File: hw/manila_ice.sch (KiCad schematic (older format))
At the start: 22 parts, among them J1 USB_B, U9 SRV05-4

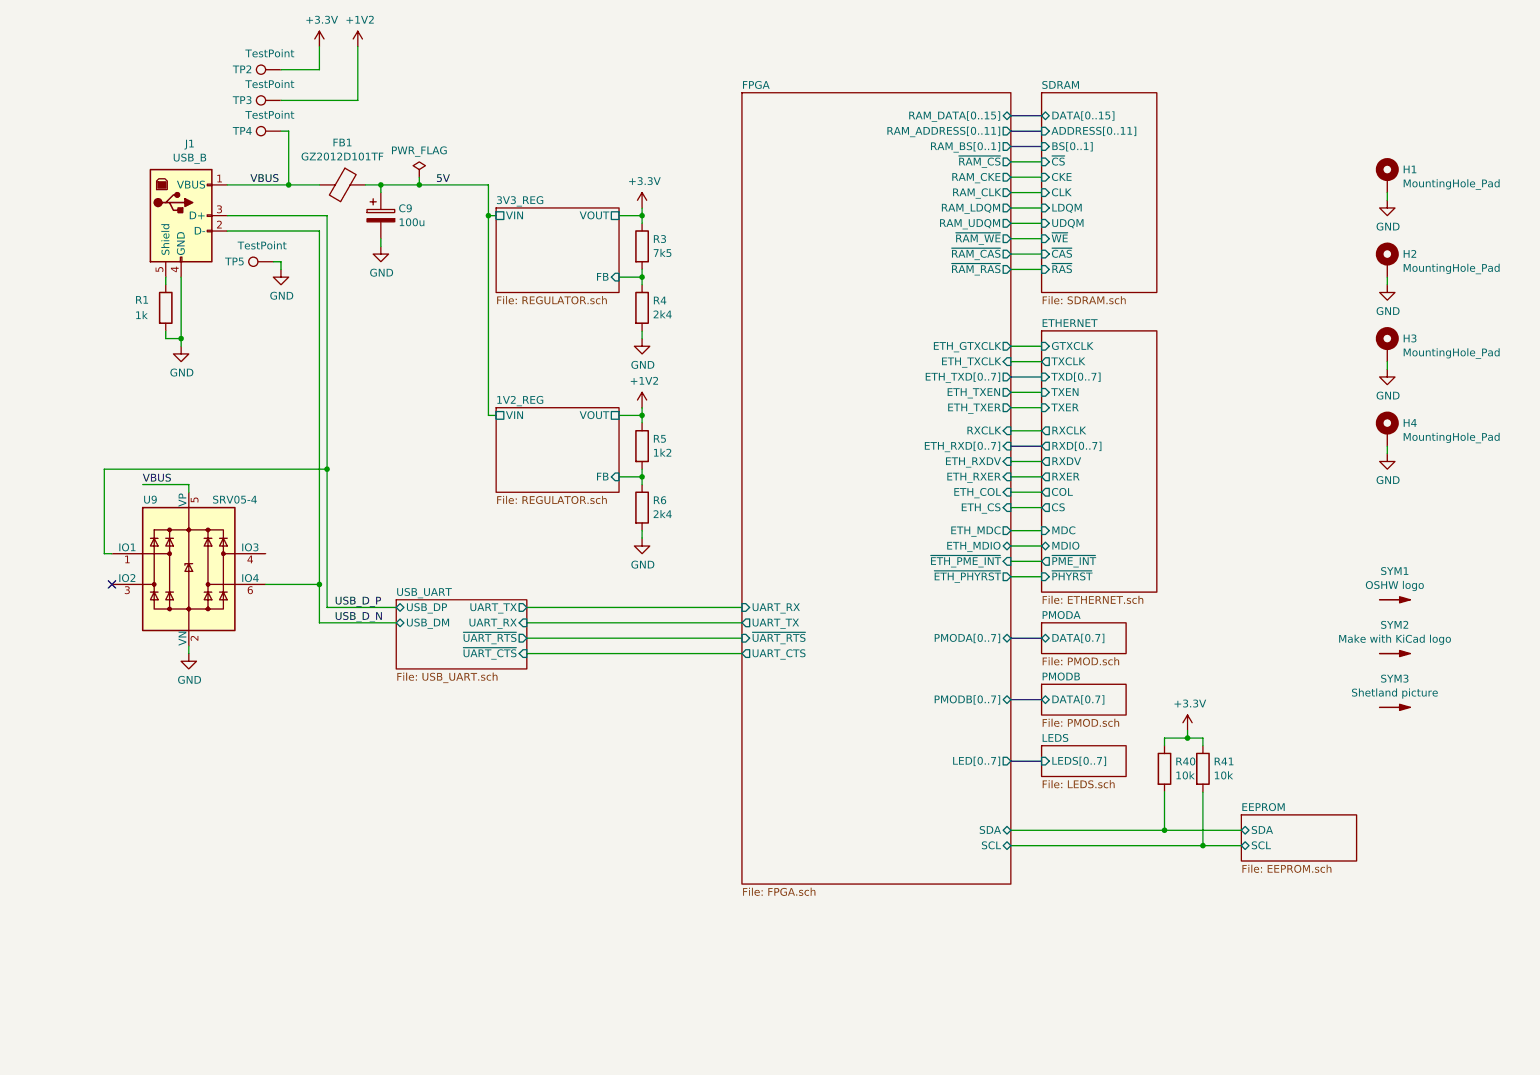
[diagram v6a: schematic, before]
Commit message: Update schematic to change slew rates of PSUs and to add switch debouncing
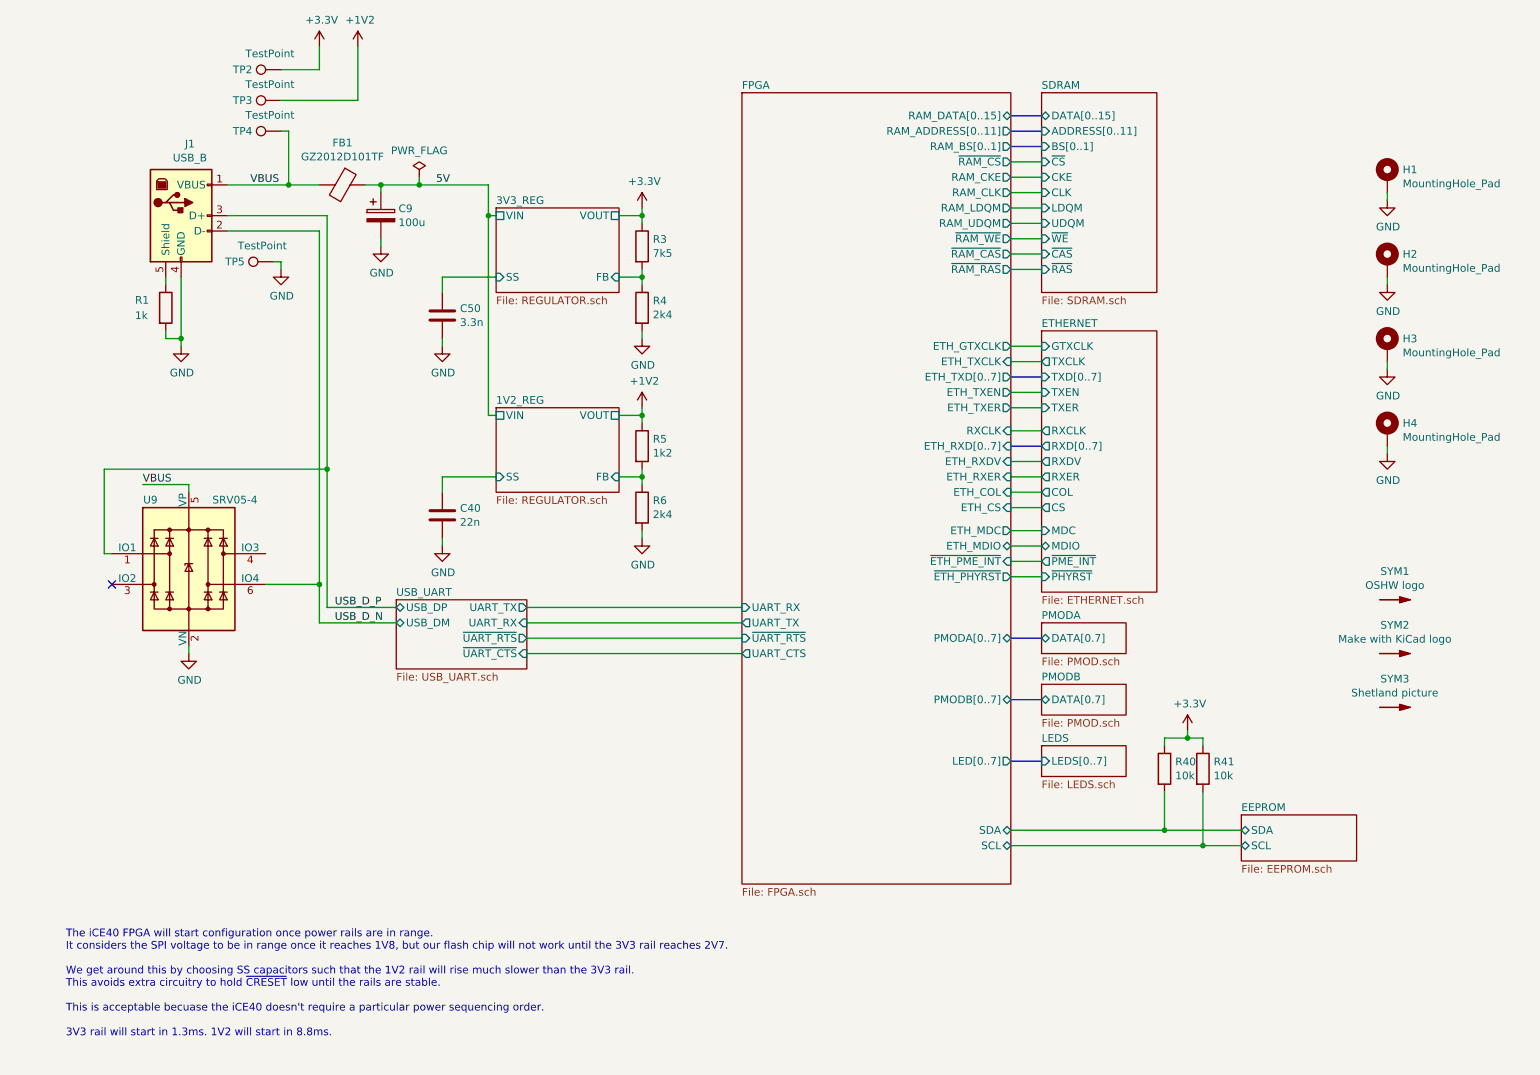
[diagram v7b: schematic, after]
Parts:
- added C40: 22n, Capacitor_SMD:C_0603_1608Metric, symbol Device:C
- added C50: 3.3n, Capacitor_SMD:C_0603_1608Metric, symbol Device:C
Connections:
- net GND: now also C40.2, C50.2
- new net 1V2_REG/SS: C40.1
- new net 3V3_REG/SS: C50.1
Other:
- note added: "The iCE40 FPGA will start configuration once power rails are in range.\nIt considers the SPI voltage to be in range once it reaches 1V8, but our flash chip will not work until the 3V3 rail reaches 2V7.\n\nWe get around this by choosing SS capacitors such that the 1V2 rail will rise much slower than the 3V3 rail.\nThis avoids extra circuitry to hold ~CRESET~ low until the rails are stable.\n\nThis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"

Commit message: Schematic tweaks
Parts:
- removed C40: 22n, Capacitor_SMD:C_0603_1608Metric, symbol Device:C
- removed C50: 3.3n, Capacitor_SMD:C_0603_1608Metric, symbol Device:C
- added R45: 360k, Resistor_SMD:R_0603_1608Metric, symbol Device:R
- added R46: 180k, Resistor_SMD:R_0603_1608Metric, symbol Device:R
- added R48: 10k, Resistor_SMD:R_0603_1608Metric, symbol Device:R
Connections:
- net +3V3: now also R45.1, R48.1
- net GND: now also R46.2
- new net 1V2_REG/EN: R45.2, R46.1
- new net EEPROM/~WC: R48.2
- no-connect marks 1 -> 2
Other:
- note added: "The iCE40 FPGA will start configuration once power rails are in range.\nIt considers the SPI voltage to be in range once it reaches 1V8, but our flash chip will not work until the 3V3 rail reaches 2V7.\n\nWe get around this by sequencing the 1V2 rail to only come up after the 3V3 is good. This avoids extra circuitry to hold ~CRESET~ low until the rails are stable.\n\nThis is acceptable becuase th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"
- note removed: "The iCE40 FPGA will start configuration once power rails are in range.\nIt considers the SPI voltage to be in range once it reaches 1V8, but our flash chip will not work until the 3V3 rail reaches 2V7.\n\nWe get around this by choosing SS capacitors such that the 1V2 rail will rise much slower than the 3V3 rail.\nThis avoids extra circuitry to hold ~CRESET~ low until the rails are stable.\n\nThis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"
- moved on the sheet: R41
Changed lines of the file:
@@
 encoding utf-8
 Sheet 1 11
-Title ""
+Title "manila iCE"
 Date ""
-Rev ""
+Rev "1.0"
 Comp ""
 Comment1 ""
@@
 F35 "SDA" B R 7000 5800 50
 F36 "SCL" B R 7000 5900 50
+F37 "~WC" O R 7000 6000 50
 $EndSheet
 $Sheet
@@
 $EndSheet
 $Sheet
-S 8500 5700 750  300
+S 8900 5700 750  400
 U 5DAA4BA2
 F0 "EEPROM" 50
 F1 "EEPROM.sch" 50
-F2 "SDA" B L 8500 5800 50
-F3 "SCL" B L 8500 5900 50
+F2 "SDA" B L 8900 5800 50
+F3 "SCL" B L 8900 5900 50
+F4 "~WC" I L 8900 6000 50
 $EndSheet
 $Sheet
@@
 F3 "VOUT" U R 4450 3100 50
 F4 "VIN" U L 3650 3100 50
-F5 "SS" I L 3650 3500 50
-$EndSheet
-$Sheet
-S 3650 1750 800  550
-U 5DB28A3C
-F0 "3V3_REG" 50
-F1 "REGULATOR.sch" 50
-F2 "FB" I R 4450 2200 50
-F3 "VOUT" U R 4450 1800 50
-F4 "VIN" U L 3650 1800 50
-F5 "SS" I L 3650 2200 50
+F5 "EN" I L 3650 3500 50
 $EndSheet
 $Comp
@@
 L Device:R R?
 U 1 1 5DAF8A15
-P 8250 5400
+P 8300 5400
 AR Path="/5D7C5FBE/5DAF8A15" Ref="R?"  Part="1"
 AR Path="/5DAF8A15" Ref="R41"  Part="1"
-F 0 "R41" H 8320 5446 50  0000 L CNN
-F 1 "10k" H 8320 5355 50  0000 L CNN
-F 2 "Resistor_SMD:R_0603_1608Metric" V 8180 5400 50  0001 C CNN
-F 3 "~" H 8250 5400 50  0001 C CNN
-F 4 "0" H 8320 5546 50  0001 C CNN "JLCPCB Rotation"
-F 5 "C25804" H 8320 5546 50  0001 C CNN "LCSC Part"
-	1    8250 5400
+F 0 "R41" H 8370 5446 50  0000 L CNN
+F 1 "10k" H 8370 5355 50  0000 L CNN
+F 2 "Resistor_SMD:R_0603_1608Metric" V 8230 5400 50  0001 C CNN
+F 3 "~" H 8300 5400 50  0001 C CNN
+F 4 "0" H 8370 5546 50  0001 C CNN "JLCPCB Rotation"
+F 5 "C25804" H 8370 5546 50  0001 C CNN "LCSC Part"
+	1    8300 5400
 	1    0    0    -1
 $EndComp
@@
 	8000 5200 8150 5200
 Wire Wire Line
-	8250 5200 8250 5250
+	8300 5200 8300 5250
 Wire Wire Line
 	8150 5150 8150 5200
 Wire Wire Line
-	8150 5200 8250 5200
+	8150 5200 8300 5200
 Wire Wire Line
 	7000 5800 8000 5800
 Wire Wire Line
-	8500 5900 8250 5900
-Wire Wire Line
 	8000 5550 8000 5800
 Wire Wire Line
-	8000 5800 8500 5800
-Wire Wire Line
-	8250 5550 8250 5900
-Wire Wire Line
-	8250 5900 7000 5900
+	8000 5800 8900 5800
 Wire Wire Line
 	4600 3900 4600 3850
@@
 Connection ~ 8150 5200
 Connection ~ 8000 5800
-Connection ~ 8250 5900
 Connection ~ 4600 3100
 Connection ~ 4600 3500
@@
 Connection ~ 2550 3450
 NoConn ~ 1150 4200
-$Comp
-L Device:C C?
-U 1 1 5DBEC469
-P 3300 3750
-AR Path="/5D7E2E67/5DBEC469" Ref="C?"  Part="1"
-AR Path="/5DAFE486/5DBEC469" Ref="C?"  Part="1"
-AR Path="/5DB28A3C/5DBEC469" Ref="C?"  Part="1"
-AR Path="/5DBEC469" Ref="C40"  Part="1"
-F 0 "C40" H 3415 3796 50  0000 L CNN
-F 1 "22n" H 3415 3705 50  0000 L CNN
-F 2 "Capacitor_SMD:C_0603_1608Metric" H 3338 3600 50  0001 C CNN
-F 3 "~" H 3300 3750 50  0001 C CNN
-F 4 "0" H 3415 3896 50  0001 C CNN "JLCPCB Rotation"
-F 5 "C21122" H 3415 3896 50  0001 C CNN "LCSC Part"
-	1    3300 3750
-	1    0    0    -1
-$EndComp
-$Comp
-L power:GND #PWR?
-U 1 1 5DBEC46F
-P 3300 3950
-AR Path="/5DBEC46F" Ref="#PWR?"  Part="1"
-AR Path="/5D7E2E67/5DBEC46F" Ref="#PWR?"  Part="1"
-AR Path="/5DAFE486/5DBEC46F" Ref="#PWR?"  Part="1"
-AR Path="/5DB28A3C/5DBEC46F" Ref="#PWR?"  Part="1"
-F 0 "#PWR?" H 3300 3700 50  0001 C CNN
-F 1 "GND" H 3305 3777 50  0000 C CNN
-F 2 "" H 3300 3950 50  0001 C CNN
-F 3 "" H 3300 3950 50  0001 C CNN
-	1    3300 3950
-	1    0    0    -1
-$EndComp
-Wire Wire Line
-	3300 3950 3300 3900
-Text Notes 850  7150 0    50   ~ 0
-The iCE40 FPGA will start configuration once power rails are in range.\nIt considers the SPI voltage to be in range once it reaches 1V8, but our flash chip will not work until the 3V3 rail reaches 2V7.\n\nWe get around this by choosing SS capacitors such that the 1V2 rail will rise much slower than the 3V3 rail.\nThis avoids extra circuitry to hold ~CRESET~ low until the rails are stable.\n\nThis is acceptable becuase the iCE40 doesn't require a particular power sequencing order.\n\n3V3 rail will start in 1.3ms. 1V2 will start in 8.8ms.
-Wire Wire Line
-	3300 3600 3300 3500
-Wire Wire Line
-	3300 3500 3650 3500
-$Comp
-L Device:C C?
-U 1 1 5DC132A2
-P 3300 2450
-AR Path="/5D7E2E67/5DC132A2" Ref="C?"  Part="1"
-AR Path="/5DAFE486/5DC132A2" Ref="C?"  Part="1"
-AR Path="/5DB28A3C/5DC132A2" Ref="C?"  Part="1"
-AR Path="/5DC132A2" Ref="C50"  Part="1"
-F 0 "C50" H 3415 2496 50  0000 L CNN
-F 1 "3.3n" H 3415 2405 50  0000 L CNN
-F 2 "Capacitor_SMD:C_0603_1608Metric" H 3338 2300 50  0001 C CNN
-F 3 "~" H 3300 2450 50  0001 C CNN
-F 4 "0" H 3415 2596 50  0001 C CNN "JLCPCB Rotation"
-F 5 "C1613" H 3415 2596 50  0001 C CNN "LCSC Part"
-	1    3300 2450
-	1    0    0    -1
-$EndComp
-$Comp
-L power:GND #PWR?
-U 1 1 5DC132A8
-P 3300 2650
-AR Path="/5DC132A8" Ref="#PWR?"  Part="1"
-AR Path="/5D7E2E67/5DC132A8" Ref="#PWR?"  Part="1"
-AR Path="/5DAFE486/5DC132A8" Ref="#PWR?"  Part="1"
-AR Path="/5DB28A3C/5DC132A8" Ref="#PWR?"  Part="1"
-F 0 "#PWR?" H 3300 2400 50  0001 C CNN
-F 1 "GND" H 3305 2477 50  0000 C CNN
-F 2 "" H 3300 2650 50  0001 C CNN
-F 3 "" H 3300 2650 50  0001 C CNN
-	1    3300 2650
-	1    0    0    -1
-$EndComp
-Wire Wire Line
-	3300 2650 3300 2600
-Wire Wire Line
-	3300 2300 3300 2200
-Wire Wire Line
-	3300 2200 3650 2200
+Text Notes 500  7300 0    50   ~ 0
+The iCE40 FPGA will start configuration once power rails are in range.\nIt considers the SPI voltage to be in range once it reaches 1V8, but our flash chip will not work until the 3V3 rail reaches 2V7.\n\nWe get around this by sequencing the 1V2 rail to only come up after the 3V3 is good. This avoids extra circuitry to hold ~CRESET~ low until the rails are stable.\n\nThis is acceptable becuase the iCE40 doesn't require a particular power sequencing order.\n\nThis works by (ab)using the EN pin of the power supply. It has hyseresis built in designed to only enable the supply when the input is in the correct voltage range.\nThe chosen resistor values turn the 1.2V supply on once the 3V3 supply is greater than 3.2V, but only turn it off again once the 3.3V supply has fallen below 2.13V.\n\nWe could probably get away without this, because the iCE40 automatically retries six times to get around power sequencing issues.\n(TN1248 p.17\nIt is best to design robustly however, and only requires two extra resistors.
+$Sheet
+S 3650 1750 800  550
+U 5DB28A3C
+F0 "3V3_REG" 50
+F1 "REGULATOR.sch" 50
+F2 "FB" I R 4450 2200 50
+F3 "VOUT" U R 4450 1800 50
+F4 "VIN" U L 3650 1800 50
+F5 "EN" I L 3650 2200 50
+$EndSheet
+NoConn ~ 3650 2200
+$Comp
+L Device:R R45
+U 1 1 5DE79830
+P 3250 3300
+F 0 "R45" H 3320 3346 50  0000 L CNN
+F 1 "360k" H 3320 3255 50  0000 L CNN
+F 2 "Resistor_SMD:R_0603_1608Metric" V 3180 3300 50  0001 C CNN
+F 3 "~" H 3250 3300 50  0001 C CNN
+F 4 "0" H 3320 3446 50  0001 C CNN "JLCPCB Rotation"
+F 5 "C23146" H 3320 3446 50  0001 C CNN "LCSC Part"
+	1    3250 3300
+	1    0    0    -1
+$EndComp
+$Comp
+L Device:R R46
+U 1 1 5DE79838
+P 3250 3700
+F 0 "R46" H 3320 3746 50  0000 L CNN
+F 1 "180k" H 3320 3655 50  0000 L CNN
+F 2 "Resistor_SMD:R_0603_1608Metric" V 3180 3700 50  0001 C CNN
+F 3 "~" H 3250 3700 50  0001 C CNN
+F 4 "0" H 3320 3846 50  0001 C CNN "JLCPCB Rotation"
+F 5 "C22827" H 3320 3846 50  0001 C CNN "LCSC Part"
+	1    3250 3700
+	1    0    0    -1
+$EndComp
+$Comp
+L power:GND #PWR0160
+U 1 1 5DE7983E
+P 3250 3900
+AR Path="/5DE7983E" Ref="#PWR0160"  Part="1"
+AR Path="/5D7E2E67/5DE7983E" Ref="#PWR?"  Part="1"
+F 0 "#PWR0160" H 3250 3650 50  0001 C CNN
+F 1 "GND" H 3255 3727 50  0000 C CNN
+F 2 "" H 3250 3900 50  0001 C CNN
+F 3 "" H 3250 3900 50  0001 C CNN
+	1    3250 3900
+	1    0    0    -1
+$EndComp
+$Comp
+L power:+3.3V #PWR0161
+U 1 1 5DE79844
+P 3250 3050
+AR Path="/5DE79844" Ref="#PWR0161"  Part="1"
+AR Path="/5D7E2E67/5DE79844" Ref="#PWR?"  Part="1"
+F 0 "#PWR0161" H 3250 2900 50  0001 C CNN
+F 1 "+3.3V" H 3265 3223 50  0000 C CNN
+F 2 "" H 3250 3050 50  0001 C CNN
+F 3 "" H 3250 3050 50  0001 C CNN
+	1    3250 3050
+	1    0    0    -1
+$EndComp
+Wire Wire Line
+	3250 3900 3250 3850
+Wire Wire Line
+	3250 3050 3250 3150
+Wire Wire Line
+	3250 3450 3250 3500
+Wire Wire Line
+	3650 3500 3250 3500
+Connection ~ 3250 3500
+Wire Wire Line
+	3250 3500 3250 3550
+$Comp
+L Device:R R?
+U 1 1 5E000C80
+P 8600 5400
+AR Path="/5D7C5FBE/5E000C80" Ref="R?"  Part="1"
+AR Path="/5E000C80" Ref="R48"  Part="1"
+F 0 "R48" H 8670 5446 50  0000 L CNN
+F 1 "10k" H 8670 5355 50  0000 L CNN
+F 2 "Resistor_SMD:R_0603_1608Metric" V 8530 5400 50  0001 C CNN
+F 3 "~" H 8600 5400 50  0001 C CNN
+F 4 "0" H 8670 5546 50  0001 C CNN "JLCPCB Rotation"
+F 5 "C25804" H 8670 5546 50  0001 C CNN "LCSC Part"
+	1    8600 5400
+	1    0    0    -1
+$EndComp
+Wire Wire Line
+	8600 5200 8600 5250
+Wire Wire Line
+	8600 5200 8300 5200
+Connection ~ 8300 5200
+Wire Wire Line
+	7000 5900 8300 5900
+Wire Wire Line
+	7000 6000 8600 6000
+Wire Wire Line
+	8300 5550 8300 5900
+Connection ~ 8300 5900
+Wire Wire Line
+	8300 5900 8900 5900
+Wire Wire Line
+	8600 5550 8600 6000
+Connection ~ 8600 6000
+Wire Wire Line
+	8600 6000 8900 6000
 $EndSCHEMATC
